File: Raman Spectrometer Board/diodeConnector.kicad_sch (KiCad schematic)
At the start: 13 parts, among them J2 Conn_01x02, Q1 AO3401A, Q2 BSS138, Q4 AO3401A, Q5 BSS138

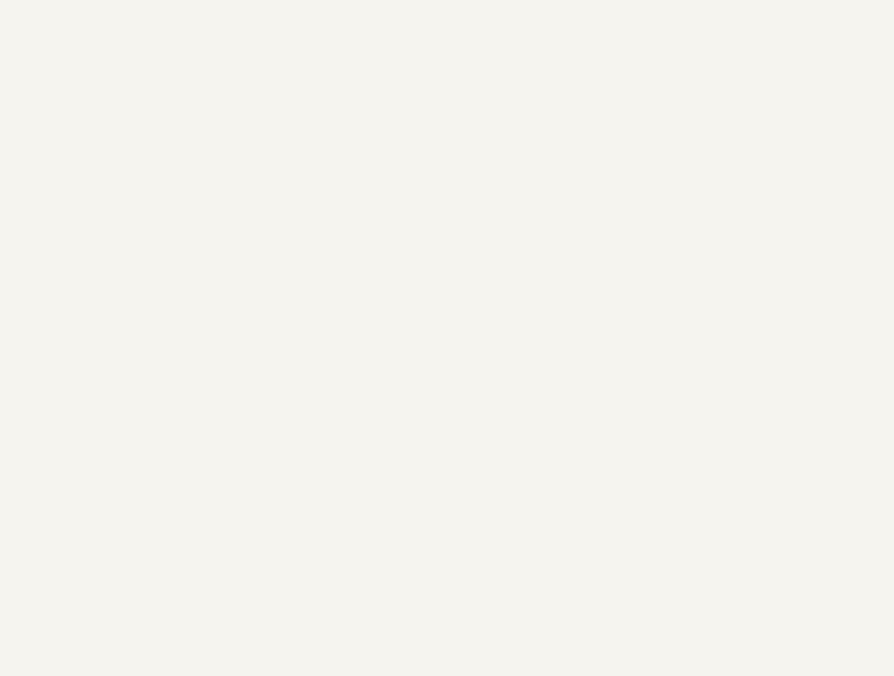
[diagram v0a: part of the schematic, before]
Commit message: limit switch connectors
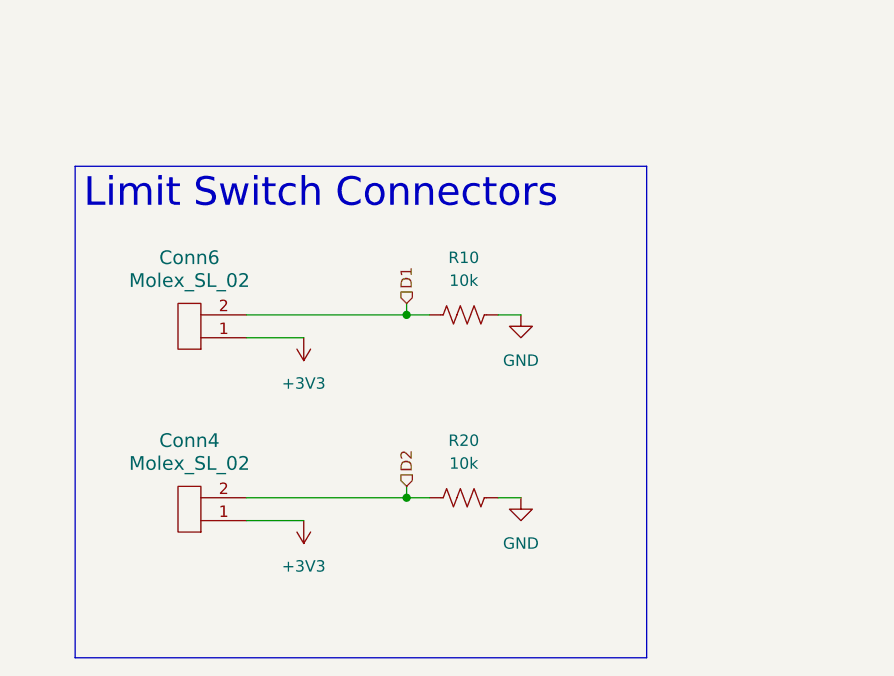
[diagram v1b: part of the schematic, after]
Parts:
- added Conn4, Conn6: Molex_SL_02, MRDT_Connectors:MOLEX_SL_02_Vertical, symbol MRDT_Connectors:Molex_SL_02
- added R10, R20: 10k, Resistor_SMD:R_0603_1608Metric_Pad0.98x0.95mm_HandSolder, symbol Device:R_US
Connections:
- net +3V3: now also Conn4.1, Conn6.1
- net GND: now also R10.2, R20.2
- new net D1: Conn6.2, R10.1
- new net D2: Conn4.2, R20.1

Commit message: Fix CDR
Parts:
- removed R10, R20: 10k, Resistor_SMD:R_0603_1608Metric_Pad0.98x0.95mm_HandSolder, symbol Device:R_US

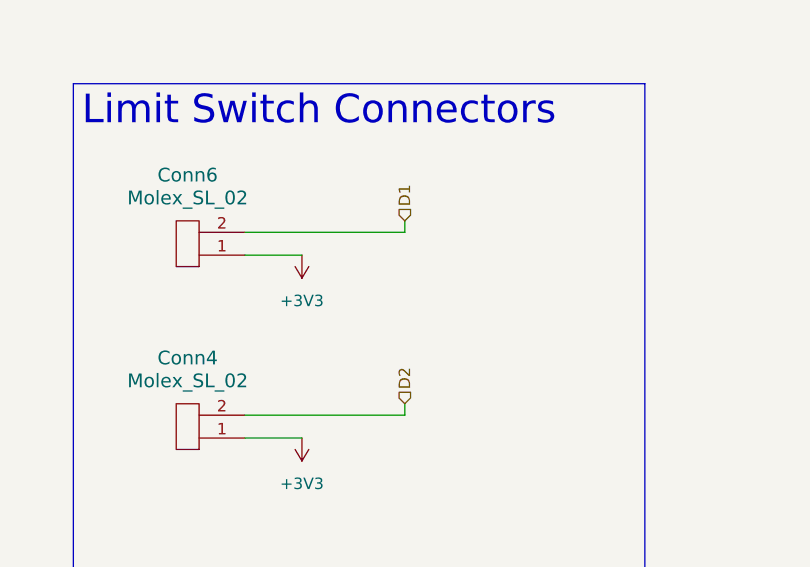
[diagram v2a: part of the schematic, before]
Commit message: Fixed switch connections
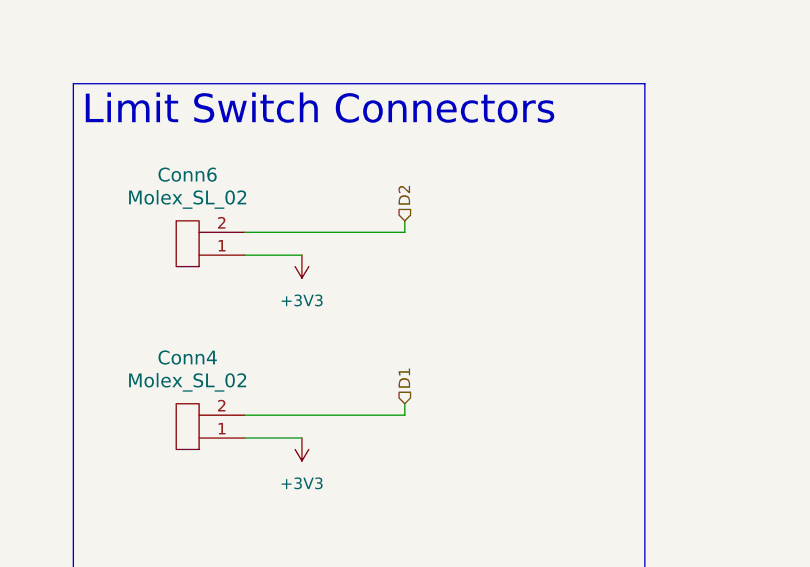
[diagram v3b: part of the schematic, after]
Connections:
- net D1: now also Conn4.2; no longer Conn6.2
- net D2: now also Conn6.2; no longer Conn4.2
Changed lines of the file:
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@@
 		)
 	)
-	(hierarchical_label "D1"
+	(hierarchical_label "D2"
 		(shape input)
 		(at 69.85 133.35 90)
@@
 		)
 	)
-	(hierarchical_label "D2"
+	(hierarchical_label "D1"
 		(shape input)
 		(at 69.85 153.67 90)

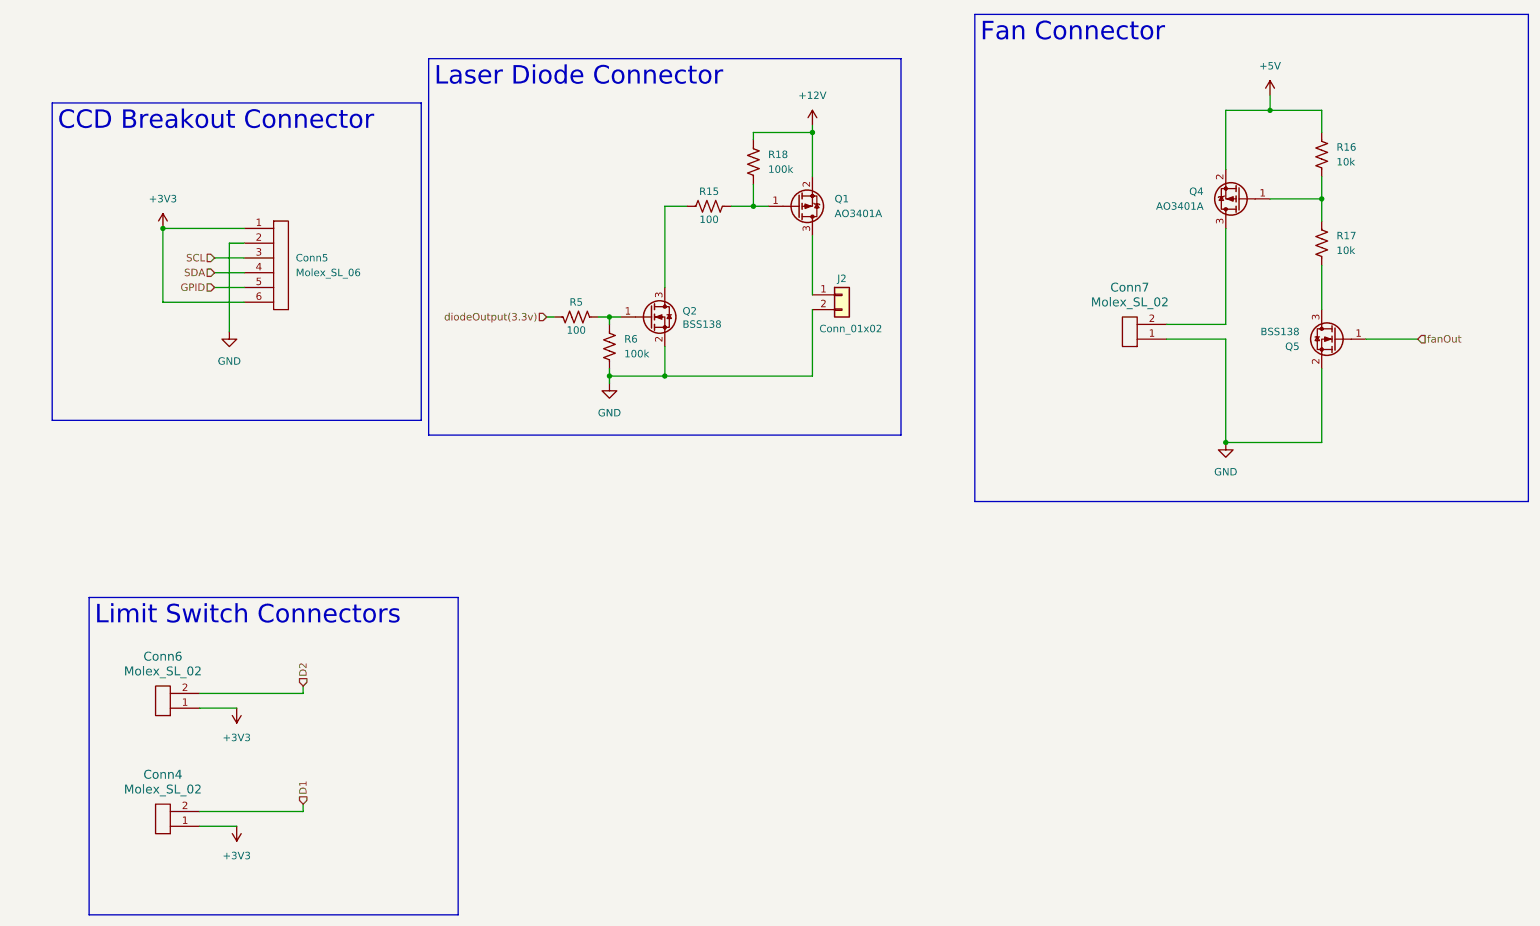
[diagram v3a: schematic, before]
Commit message: Added laser driver sheet
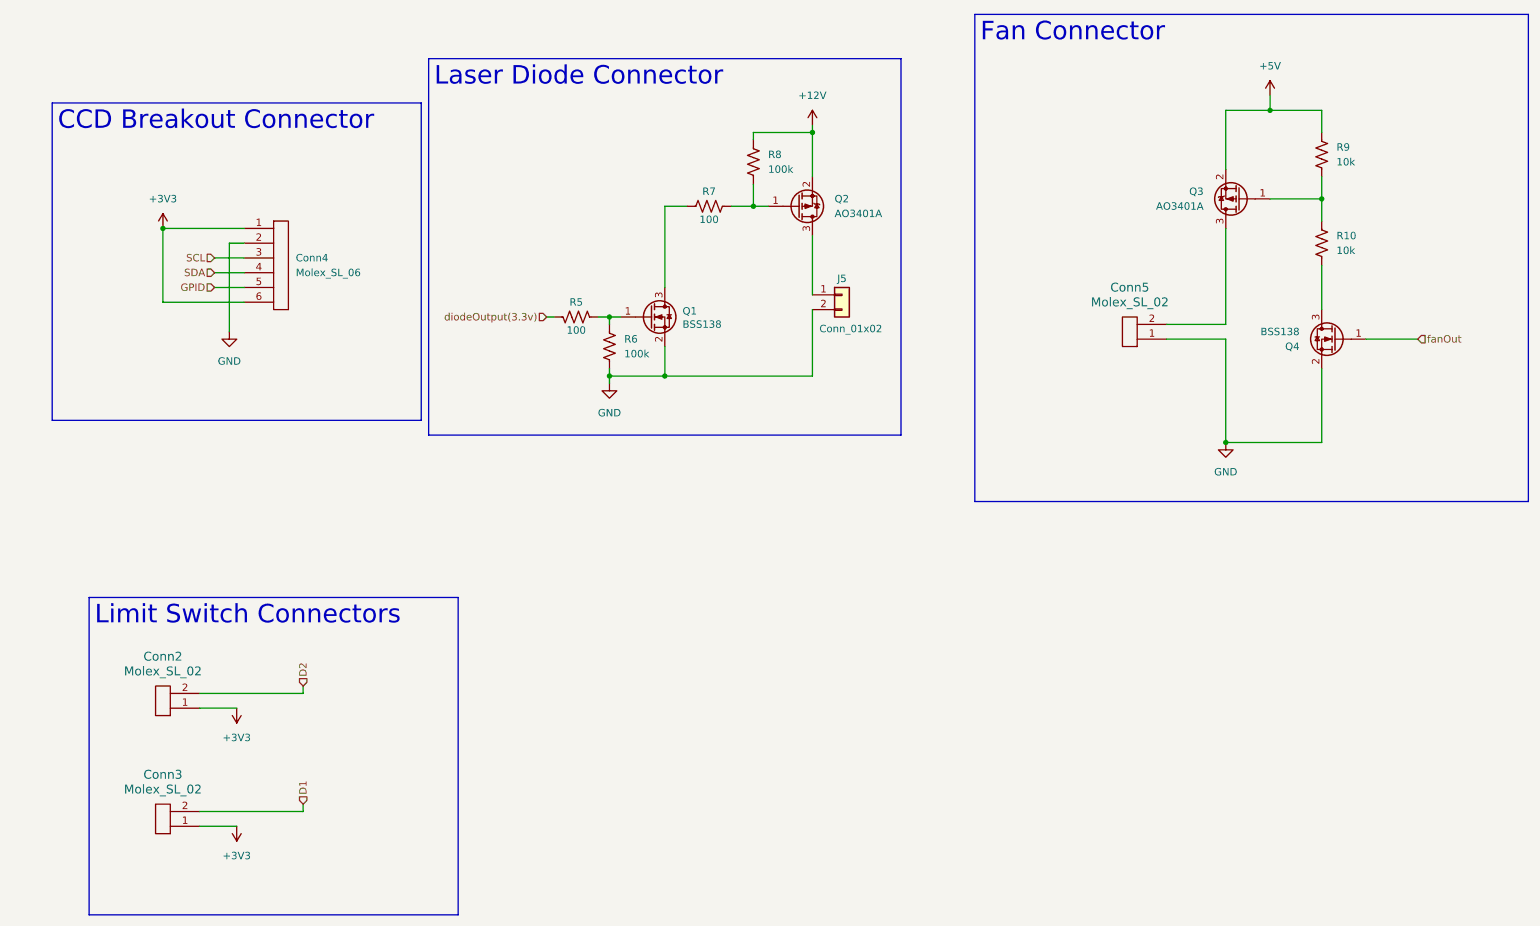
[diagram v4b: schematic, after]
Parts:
- renumbered Conn6 to Conn2, Conn4 to Conn3, Conn5 to Conn4, Conn7 to Conn5, J2 to J5, Q2 to Q1, Q1 to Q2, Q4 to Q3, Q5 to Q4, R17 to R10, R15 to R7, R18 to R8, R16 to R9
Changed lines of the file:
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@@
 		(dnp no)
 		(fields_autoplaced yes)
-		(property "Reference" "#PWR038"
+		(property "Reference" "#PWR029"
 			(at 228.6 97.79 0)
 			(effects
@@
 			(project "RamanSpectrometerBoard"
 				(path "/ab487c59-f066-48f5-a383-99e8eaf806bf/c790a08a-952a-47a5-8a2d-3628381b83e8"
-					(reference "#PWR038")
+					(reference "#PWR029")
 					(unit 1)
 				)
@@
 		(on_board yes)
 		(dnp no)
-		(property "Reference" "J2"
+		(property "Reference" "J5"
 			(at 162.56 63.246 0)
 			(effects
@@
 			(project "RamanSpectrometerBoard"
 				(path "/ab487c59-f066-48f5-a383-99e8eaf806bf/c790a08a-952a-47a5-8a2d-3628381b83e8"
-					(reference "J2")
+					(reference "J5")
 					(unit 1)
 				)
@@
 		(dnp no)
 		(fields_autoplaced yes)
-		(property "Reference" "Conn6"
+		(property "Reference" "Conn2"
 			(at 45.72 128.27 0)
 			(effects
@@
 			(project "RamanSpectrometerBoard"
 				(path "/ab487c59-f066-48f5-a383-99e8eaf806bf/c790a08a-952a-47a5-8a2d-3628381b83e8"
-					(reference "Conn6")
+					(reference "Conn2")
 					(unit 1)
 				)
@@
 		(dnp no)
 		(fields_autoplaced yes)
-		(property "Reference" "Conn7"
+		(property "Reference" "Conn5"
 			(at 212.09 64.77 0)
 			(effects
@@
 			(project ""
 				(path "/ab487c59-f066-48f5-a383-99e8eaf806bf/c790a08a-952a-47a5-8a2d-3628381b83e8"
-					(reference "Conn7")
+					(reference "Conn5")
 					(unit 1)
 				)
@@
 		(dnp no)
 		(fields_autoplaced yes)
-		(property "Reference" "Q4"
+		(property "Reference" "Q3"
 			(at 224.79 48.2599 0)
 			(effects
@@
 			(project "RamanSpectrometerBoard"
 				(path "/ab487c59-f066-48f5-a383-99e8eaf806bf/c790a08a-952a-47a5-8a2d-3628381b83e8"
-					(reference "Q4")
+					(reference "Q3")
 					(unit 1)
 				)
@@
 		(dnp no)
 		(fields_autoplaced yes)
-		(property "Reference" "#PWR049"
+		(property "Reference" "#PWR030"
 			(at 236.22 35.56 0)
 			(effects
@@
 			(project ""
 				(path "/ab487c59-f066-48f5-a383-99e8eaf806bf/c790a08a-952a-47a5-8a2d-3628381b83e8"
-					(reference "#PWR049")
+					(reference "#PWR030")
 					(unit 1)
 				)
@@
 		(on_board yes)
 		(dnp no)
-		(property "Reference" "Q2"
+		(property "Reference" "Q1"
 			(at 135.128 68.8341 0)
 			(effects
@@
 			(project "RamanSpectrometerBoard"
 				(path "/ab487c59-f066-48f5-a383-99e8eaf806bf/c790a08a-952a-47a5-8a2d-3628381b83e8"
-					(reference "Q2")
+					(reference "Q1")
 					(unit 1)
 				)
@@
 		(dnp no)
 		(fields_autoplaced yes)
-		(property "Reference" "#PWR030"
+		(property "Reference" "#PWR023"
 			(at 45.72 58.42 0)
 			(effects
@@
 			(project "RamanSpectrometerBoard"
 				(path "/ab487c59-f066-48f5-a383-99e8eaf806bf/c790a08a-952a-47a5-8a2d-3628381b83e8"
-					(reference "#PWR030")
+					(reference "#PWR023")
 					(unit 1)
 				)
@@
 		(dnp no)
 		(fields_autoplaced yes)
-		(property "Reference" "#PWR051"
+		(property "Reference" "#PWR026"
 			(at 58.42 153.67 0)
 			(effects
@@
 			(project "RamanSpectrometerBoard"
 				(path "/ab487c59-f066-48f5-a383-99e8eaf806bf/c790a08a-952a-47a5-8a2d-3628381b83e8"
-					(reference "#PWR051")
+					(reference "#PWR026")
 					(unit 1)
 				)
@@
 		(dnp no)
 		(fields_autoplaced yes)
-		(property "Reference" "#PWR052"
+		(property "Reference" "#PWR025"
 			(at 58.42 133.35 0)
 			(effects
@@
 			(project "RamanSpectrometerBoard"
 				(path "/ab487c59-f066-48f5-a383-99e8eaf806bf/c790a08a-952a-47a5-8a2d-3628381b83e8"
-					(reference "#PWR052")
+					(reference "#PWR025")
 					(unit 1)
 				)
@@
 		(on_board yes)
 		(dnp no)
-		(property "Reference" "Q5"
+		(property "Reference" "Q4"
 			(at 241.3 74.9301 0)
 			(effects
@@
 			(project "RamanSpectrometerBoard"
 				(path "/ab487c59-f066-48f5-a383-99e8eaf806bf/c790a08a-952a-47a5-8a2d-3628381b83e8"
-					(reference "Q5")
+					(reference "Q4")
 					(unit 1)
 				)
@@
 		(on_board yes)
 		(dnp no)
-		(property "Reference" "R15"
+		(property "Reference" "R7"
 			(at 139.7 48.26 90)
 			(effects
@@
 			(project "RamanSpectrometerBoard"
 				(path "/ab487c59-f066-48f5-a383-99e8eaf806bf/c790a08a-952a-47a5-8a2d-3628381b83e8"
-					(reference "R15")
+					(reference "R7")
 					(unit 1)
 				)
@@
 		(dnp no)
 		(fields_autoplaced yes)
-		(property "Reference" "Conn4"
+		(property "Reference" "Conn3"
 			(at 45.72 148.59 0)
 			(effects
@@
 			(project "RamanSpectrometerBoard"
 				(path "/ab487c59-f066-48f5-a383-99e8eaf806bf/c790a08a-952a-47a5-8a2d-3628381b83e8"
-					(reference "Conn4")
+					(reference "Conn3")
 					(unit 1)
 				)
@@
 		(on_board yes)
 		(dnp no)
-		(property "Reference" "R18"
+		(property "Reference" "R8"
 			(at 149.86 41.9099 0)
 			(effects
@@
 			(project "RamanSpectrometerBoard"
 				(path "/ab487c59-f066-48f5-a383-99e8eaf806bf/c790a08a-952a-47a5-8a2d-3628381b83e8"
-					(reference "R18")
+					(reference "R8")
 					(unit 1)
 				)
@@
 		(dnp no)
 		(fields_autoplaced yes)
-		(property "Reference" "Q1"
+		(property "Reference" "Q2"
 			(at 161.29 49.5299 0)
 			(effects
@@
 			(project "RamanSpectrometerBoard"
 				(path "/ab487c59-f066-48f5-a383-99e8eaf806bf/c790a08a-952a-47a5-8a2d-3628381b83e8"
-					(reference "Q1")
+					(reference "Q2")
 					(unit 1)
 				)
@@
 		(dnp no)
 		(fields_autoplaced yes)
-		(property "Reference" "#PWR024"
+		(property "Reference" "#PWR027"
 			(at 122.555 87.63 0)
 			(effects
@@
 			(project "RamanSpectrometerBoard"
 				(path "/ab487c59-f066-48f5-a383-99e8eaf806bf/c790a08a-952a-47a5-8a2d-3628381b83e8"
-					(reference "#PWR024")
+					(reference "#PWR027")
 					(unit 1)
 				)
@@
 		(dnp no)
 		(fields_autoplaced yes)
-		(property "Reference" "R17"
+		(property "Reference" "R10"
 			(at 247.65 55.8799 0)
 			(effects
@@
 			(project "RamanSpectrometerBoard"
 				(path "/ab487c59-f066-48f5-a383-99e8eaf806bf/c790a08a-952a-47a5-8a2d-3628381b83e8"
-					(reference "R17")
+					(reference "R10")
 					(unit 1)
 				)
@@
 		(dnp no)
 		(fields_autoplaced yes)
-		(property "Reference" "#PWR039"
+		(property "Reference" "#PWR024"
 			(at 57.15 78.74 0)
 			(effects
@@
 			(project "RamanSpectrometerBoard"
 				(path "/ab487c59-f066-48f5-a383-99e8eaf806bf/c790a08a-952a-47a5-8a2d-3628381b83e8"
-					(reference "#PWR039")
+					(reference "#PWR024")
 					(unit 1)
 				)
@@
 		(dnp no)
 		(fields_autoplaced yes)
-		(property "Reference" "Conn5"
+		(property "Reference" "Conn4"
 			(at 68.58 59.6899 0)
 			(effects
@@
 			(project ""
 				(path "/ab487c59-f066-48f5-a383-99e8eaf806bf/c790a08a-952a-47a5-8a2d-3628381b83e8"
-					(reference "Conn5")
+					(reference "Conn4")
 					(unit 1)
 				)
@@
 		(dnp no)
 		(fields_autoplaced yes)
-		(property "Reference" "R16"
+		(property "Reference" "R9"
 			(at 247.65 40.6399 0)
 			(effects
@@
 			(project "RamanSpectrometerBoard"
 				(path "/ab487c59-f066-48f5-a383-99e8eaf806bf/c790a08a-952a-47a5-8a2d-3628381b83e8"
-					(reference "R16")
+					(reference "R9")
 					(unit 1)
 				)
@@
 		(dnp no)
 		(fields_autoplaced yes)
-		(property "Reference" "#PWR025"
+		(property "Reference" "#PWR028"
 			(at 157.48 40.64 0)
 			(effects
@@
 			(project ""
 				(path "/ab487c59-f066-48f5-a383-99e8eaf806bf/c790a08a-952a-47a5-8a2d-3628381b83e8"
-					(reference "#PWR025")
-					(unit 1)
-				)
+					(reference "#PWR028")
+					(unit 1)
+				)

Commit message: Delete Extras
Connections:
- net +3V3: now also Conn4.5; no longer Conn4.6
- net GPID: now also Conn4.6; no longer Conn4.5
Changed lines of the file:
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@@
 	(wire
 		(pts
-			(xy 45.72 54.61) (xy 45.72 67.31)
+			(xy 45.72 54.61) (xy 45.72 64.77)
 		)
 		(stroke
@@
 	(wire
 		(pts
-			(xy 54.61 64.77) (xy 59.69 64.77)
+			(xy 54.61 67.31) (xy 59.69 67.31)
 		)
 		(stroke
@@
 	(wire
 		(pts
+			(xy 45.72 64.77) (xy 59.69 64.77)
+		)
+		(stroke
+			(width 0)
+			(type default)
+		)
+	)
+	(wire
+		(pts
 			(xy 228.6 73.66) (xy 228.6 91.44)
 		)
@@
 		(pts
 			(xy 54.61 59.69) (xy 59.69 59.69)
-		)
-		(stroke
-			(width 0)
-			(type default)
-		)
-	)
-	(wire
-		(pts
-			(xy 59.69 67.31) (xy 45.72 67.31)
 		)
 		(stroke
@@
 	(hierarchical_label "GPID"
 		(shape input)
-		(at 54.61 64.77 180)
+		(at 54.61 67.31 180)
 		(effects
 			(font
